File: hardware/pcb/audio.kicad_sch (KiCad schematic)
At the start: 7 parts, among them IC3 TAC5212, J6 PJ-342

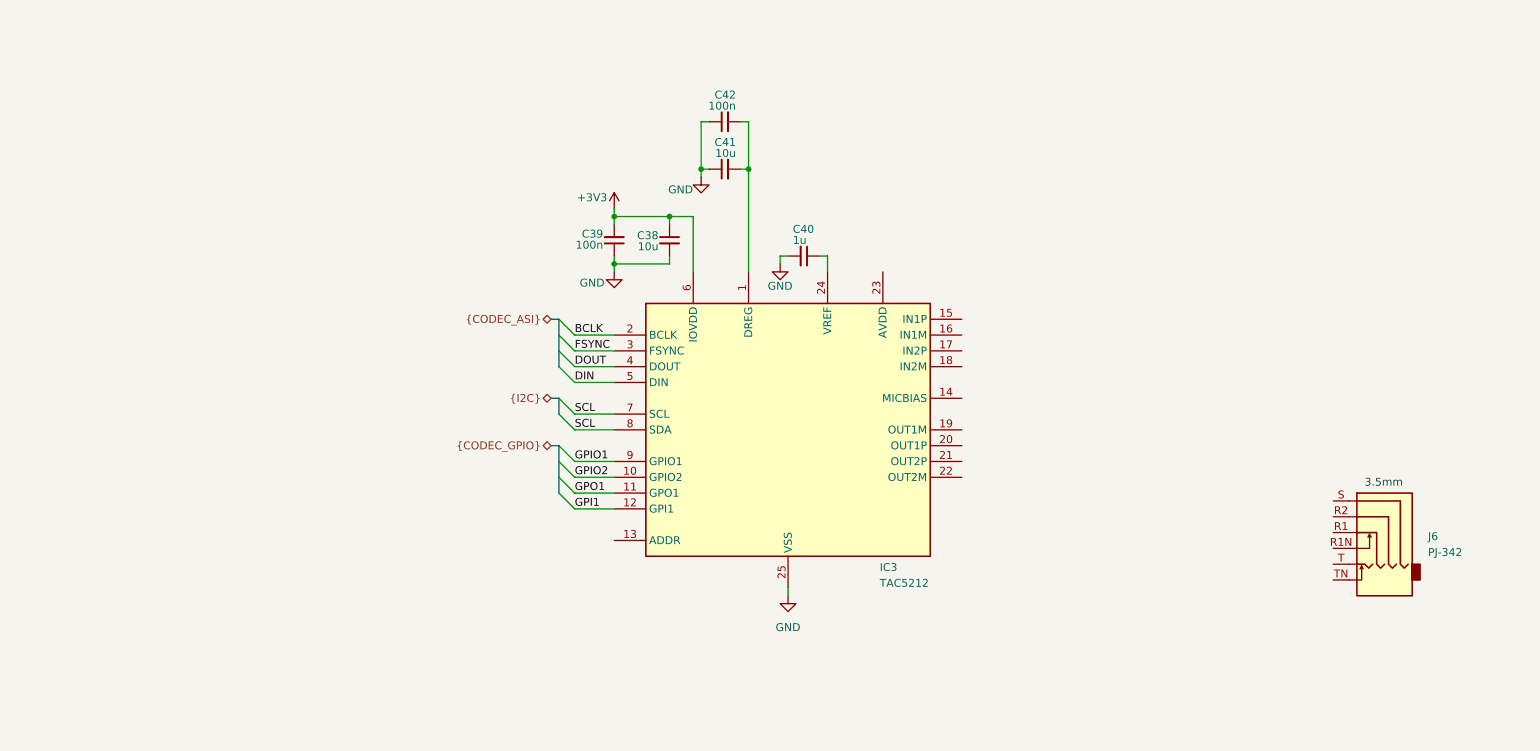
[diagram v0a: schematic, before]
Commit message: bunch of small audio changes
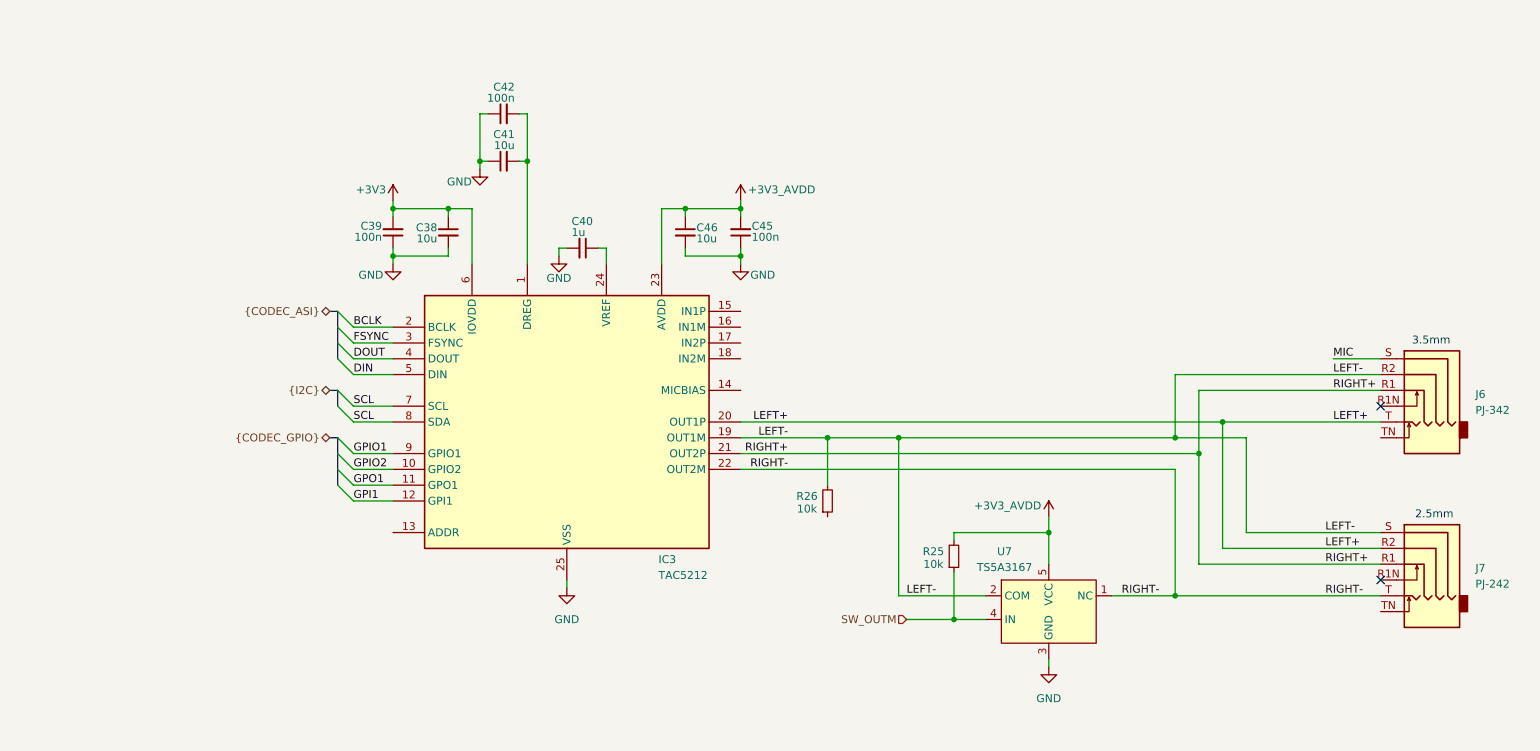
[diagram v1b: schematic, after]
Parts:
- added C45: 100n, symbol Device:C_Small
- added C46: 10u, symbol Device:C_Small
- added J7: PJ-242, PJ242:Jack_2.5mm_PJ242_6P_12x6.2x4mm_Horizontal, symbol Connector_Audio:AudioJack4_SwitchTR1
- added R25, R26: 10k, symbol Device:R_Small
- added U7: TS5A3167, Package_TO_SOT_SMD:SOT-23-5, symbol TS5A3167:TS5A3167
- J6: LCSC (none) -> C668606
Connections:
- net GND: now also C45.1, C46.2, U7.3 (GND)
- net RIGHT+: now reaches J6.R1
- net RIGHT+: now also IC3.21 (OUT2P), J7.R1
- net LEFT-: now reaches J6.R2
- net LEFT-: now also IC3.19 (OUT1M), J7.S, R26.2, U7.2 (COM)
- net MIC: now reaches J6.S
- net LEFT+: now reaches J6.T
- net LEFT+: now also IC3.20 (OUT1P), J7.R2
- net RIGHT-: now reaches IC3.22 (OUT2M)
- net RIGHT-: now also J7.T, U7.1 (NC)
- net +3V3_AVDD: now reaches IC3.23 (AVDD)
- net +3V3_AVDD: now also C45.2, C46.1, R25.2, U7.5 (VCC)
- new net SW_OUTM: R25.1, U7.4 (IN)
- no-connect marks 0 -> 2
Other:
- note added: "2.5mm"
- moved on the sheet: C38, C39, C40, C41, C42, IC3, J6

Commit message: bunch of small audio changes
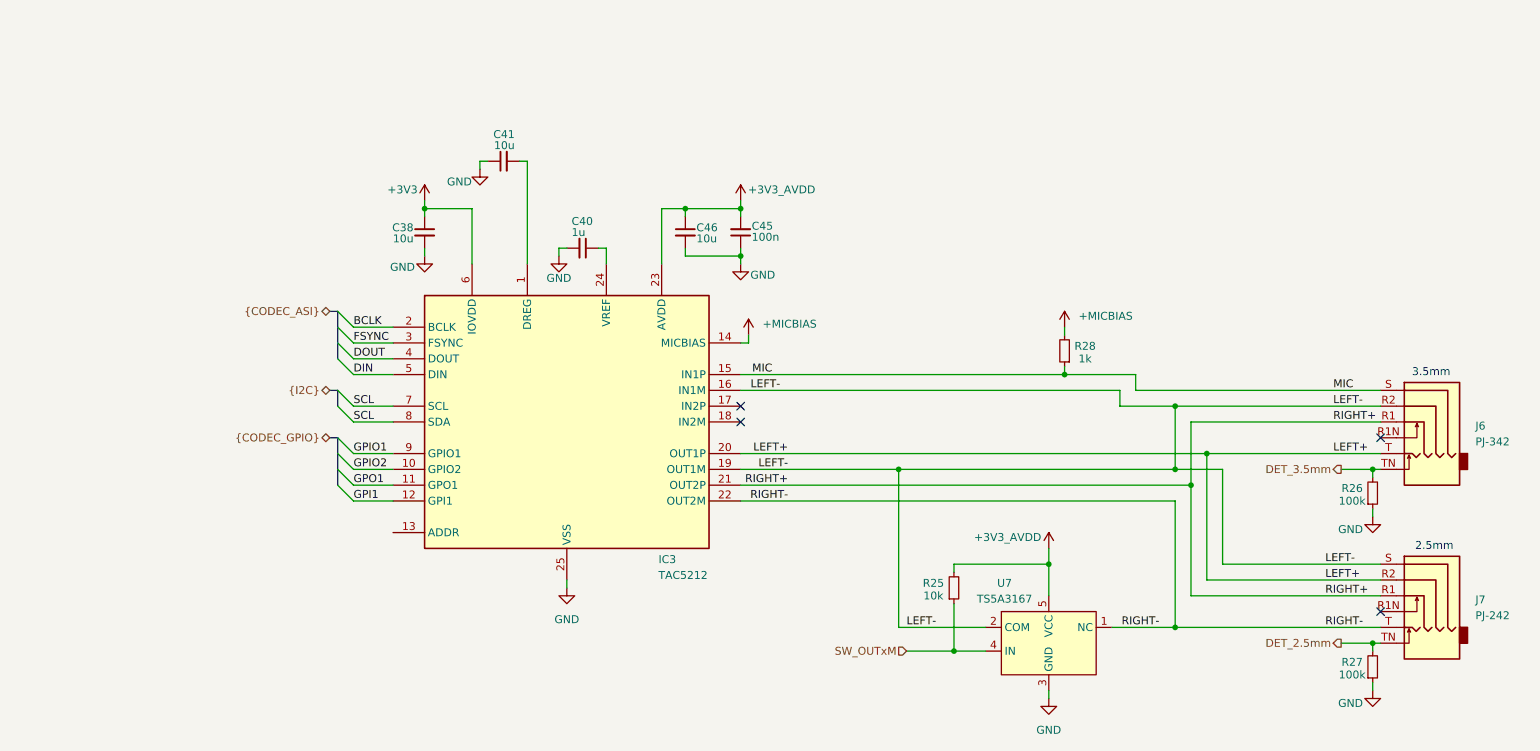
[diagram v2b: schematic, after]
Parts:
- removed C39, C42: 100n, symbol Device:C_Small
- added R27: 100k, symbol Device:R_Small
- added R28: 1k, symbol Device:R_Small
- R26: value 10k -> 100k
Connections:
- net GND: now also R26.1, R27.1
- net LEFT-: now also IC3.16 (IN1M); no longer R26.2
- net MIC: now also IC3.15 (IN1P), R28.1
- net DET_2.5mm: now reaches J7.TN
- net DET_2.5mm: now also R27.2
- net DET_3.5mm: now reaches J6.TN
- net DET_3.5mm: now also R26.2
- net +MICBIAS: now reaches IC3.14 (MICBIAS)
- net +MICBIAS: now also R28.2
- net SW_OUTM renamed SW_OUTxM
- no-connect marks 2 -> 4
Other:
- moved on the sheet: C38, J6, J7, R25, U7

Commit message: bunch of small audio and rf changes
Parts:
- removed C45: 100n, symbol Device:C_Small
- C38, C41: value 10u -> 1u
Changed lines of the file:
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@@
 	)
 	(junction
-		(at 134.62 58.42)
-		(diameter 0)
-		(color 0 0 0 0)
-	)
-	(junction
 		(at 204.47 92.71)
 		(diameter 0)
@@
 	)
 	(junction
-		(at 134.62 50.8)
-		(diameter 0)
-		(color 0 0 0 0)
-	)
-	(junction
 		(at 209.55 90.17)
 		(diameter 0)
@@
 	(wire
 		(pts
-			(xy 134.62 57.15) (xy 134.62 58.42)
-		)
-		(stroke
-			(width 0)
-			(type default)
-		)
-	)
-	(wire
-		(pts
 			(xy 134.62 92.71) (xy 160.02 92.71)
 		)
@@
 	(wire
 		(pts
-			(xy 134.62 49.53) (xy 134.62 50.8)
+			(xy 125.73 49.53) (xy 125.73 50.8)
 		)
 		(stroke
@@
 	(wire
 		(pts
-			(xy 125.73 58.42) (xy 125.73 57.15)
+			(xy 125.73 57.15) (xy 125.73 58.42)
 		)
 		(stroke
@@
 	(wire
 		(pts
-			(xy 134.62 59.69) (xy 134.62 58.42)
-		)
-		(stroke
-			(width 0)
-			(type default)
-		)
-	)
-	(wire
-		(pts
 			(xy 231.14 92.71) (xy 236.22 92.71)
 		)
@@
 		)
 	)
-	(wire
-		(pts
-			(xy 134.62 50.8) (xy 134.62 52.07)
-		)
-		(stroke
-			(width 0)
-			(type default)
-		)
-	)
 	(bus
 		(pts
@@
 	(wire
 		(pts
-			(xy 125.73 50.8) (xy 134.62 50.8)
-		)
-		(stroke
-			(width 0)
-			(type default)
-		)
-	)
-	(wire
-		(pts
 			(xy 207.01 85.09) (xy 237.49 85.09)
 		)
@@
 		)
 	)
-	(wire
-		(pts
-			(xy 134.62 58.42) (xy 125.73 58.42)
-		)
-		(stroke
-			(width 0)
-			(type default)
-		)
-	)
 	(bus
 		(pts
@@
 		)
 	)
-	(hierarchical_label "{CODEC_ASI}"
+	(hierarchical_label "{ASI}"
 		(shape bidirectional)
 		(at 68.58 67.31 180)
@@
 			)
 		)
-		(property "Value" "10u"
+		(property "Value" "1u"
 			(at 98.298 40.64 90)
 			(show_name no)
@@
 	(symbol
 		(lib_id "power:+3V3")
-		(at 134.62 49.53 0)
+		(at 125.73 49.53 0)
 		(unit 1)
 		(body_style 1)
@@
 		(dnp no)
 		(property "Reference" "#PWR094"
-			(at 134.62 53.34 0)
+			(at 125.73 53.34 0)
 			(hide yes)
 			(show_name no)
@@
 		)
 		(property "Value" "+3V3_AVDD"
-			(at 141.224 47.752 0)
+			(at 132.334 47.752 0)
 			(show_name no)
 			(do_not_autoplace no)
@@
 		)
 		(property "Footprint" ""
-			(at 134.62 49.53 0)
+			(at 125.73 49.53 0)
 			(hide yes)
 			(show_name no)
@@
 		)
 		(property "Datasheet" ""
-			(at 134.62 49.53 0)
+			(at 125.73 49.53 0)
 			(hide yes)
 			(show_name no)
@@
 		)
 		(property "Description" "Power symbol creates a global label with name \"+3V3\""
-			(at 134.62 49.53 0)
+			(at 125.73 49.53 0)
 			(hide yes)
 			(show_name no)
@@
 			)
 		)
-		(property "Value" "10u"
+		(property "Value" "1u"
 			(at 82.042 55.626 0)
 			(show_name no)
@@
 	(symbol
 		(lib_id "power:GND")
-		(at 134.62 59.69 0)
+		(at 125.73 58.42 0)
 		(mirror y)
 		(unit 1)
@@
 		(dnp no)
 		(property "Reference" "#PWR096"
-			(at 134.62 66.04 0)
+			(at 125.73 64.77 0)
 			(hide yes)
 			(show_name no)
@@
 		)
 		(property "Value" "GND"
-			(at 138.176 61.468 0)
+			(at 129.286 60.198 0)
 			(show_name no)
 			(do_not_autoplace no)
@@
 		)
 		(property "Footprint" ""
-			(at 134.62 59.69 0)
+			(at 125.73 58.42 0)
 			(hide yes)
 			(show_name no)
@@
 		)
 		(property "Datasheet" ""
-			(at 134.62 59.69 0)
+			(at 125.73 58.42 0)
 			(hide yes)
 			(show_name no)
@@
 		)
 		(property "Description" "Power symbol creates a global label with name \"GND\" , ground"
-			(at 134.62 59.69 0)
+			(at 125.73 58.42 0)
 			(hide yes)
 			(show_name no)
@@
 					(unit 1)
 				)
-			)
-		)
-	)
-	(symbol
-		(lib_id "Device:C_Small")
-		(at 134.62 54.61 0)
-		(mirror x)
-		(unit 1)
-		(body_style 1)
-		(exclude_from_sim no)
-		(in_bom yes)
-		(on_board yes)
-		(in_pos_files yes)
-		(dnp no)
-		(property "Reference" "C45"
-			(at 136.398 53.594 0)
-			(show_name no)
-			(do_not_autoplace no)
-			(effects
-				(font
-					(size 1.27 1.27)
-				)
-				(justify left)
-			)
-		)
-		(property "Value" "100n"
-			(at 136.398 55.372 0)
-			(show_name no)
-			(do_not_autoplace no)
-			(effects
-				(font
-					(size 1.27 1.27)
-				)
-				(justify left)
-			)
-		)
-		(property "Footprint" ""
-			(at 134.62 54.61 0)
-			(hide yes)
-			(show_name no)
-			(do_not_autoplace no)
-			(effects
-				(font
-					(size 1.27 1.27)
-				)
-			)
-		)
-		(property "Datasheet" ""
-			(at 134.62 54.61 0)
-			(hide yes)
-			(show_name no)
-			(do_not_autoplace no)
-			(effects
-				(font
-					(size 1.27 1.27)
-				)
-			)
-		)
-		(property "Description" "Unpolarized capacitor, small symbol"
-			(at 134.62 54.61 0)
-			(hide yes)
-			(show_name no)
-			(do_not_autoplace no)
-			(effects
-				(font
-					(size 1.27 1.27)
-				)
-			)
-		)
-		(property "KLC_S3.3" ""
-			(at 134.62 54.61 90)
-			(hide yes)
-			(show_name no)
-			(do_not_autoplace no)
-			(effects
-				(font
-					(size 1.27 1.27)
-				)
-			)
-		)
-		(property "KLC_S4.1" ""
-			(at 134.62 54.61 90)
-			(hide yes)
-			(show_name no)
-			(do_not_autoplace no)
-			(effects
-				(font
-					(size 1.27 1.27)
-				)
-			)
-		)
-		(pin "1"
-		)
-		(pin "2"
-		)
-		(instances
-			(project "meko"
-				(path "/da54f10a-146b-4941-a9c7-55c7173bb101/073f6085-34ed-486a-9dc9-0ac1ede2fab6"
-					(reference "C45")
-					(unit 1)
-				)

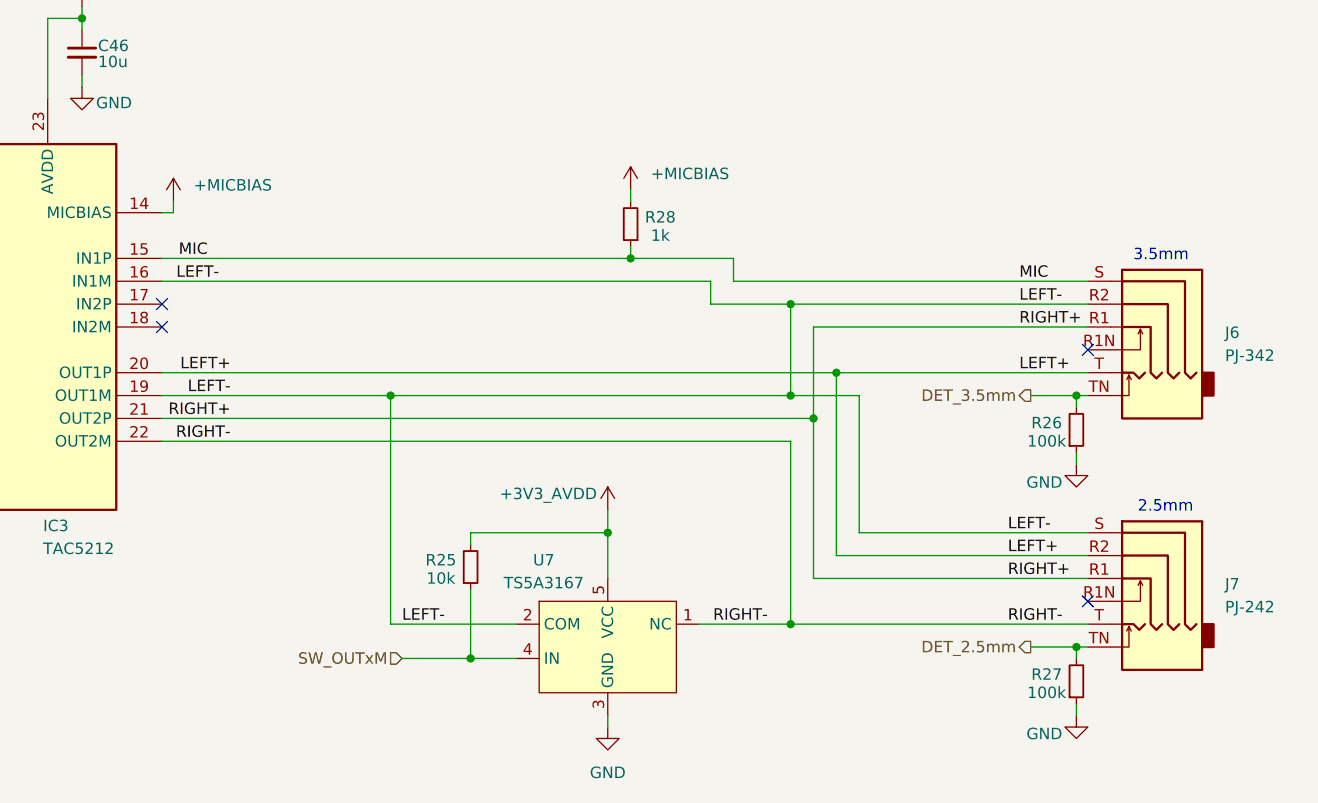
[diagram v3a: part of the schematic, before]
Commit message: removed analog switch from audio path
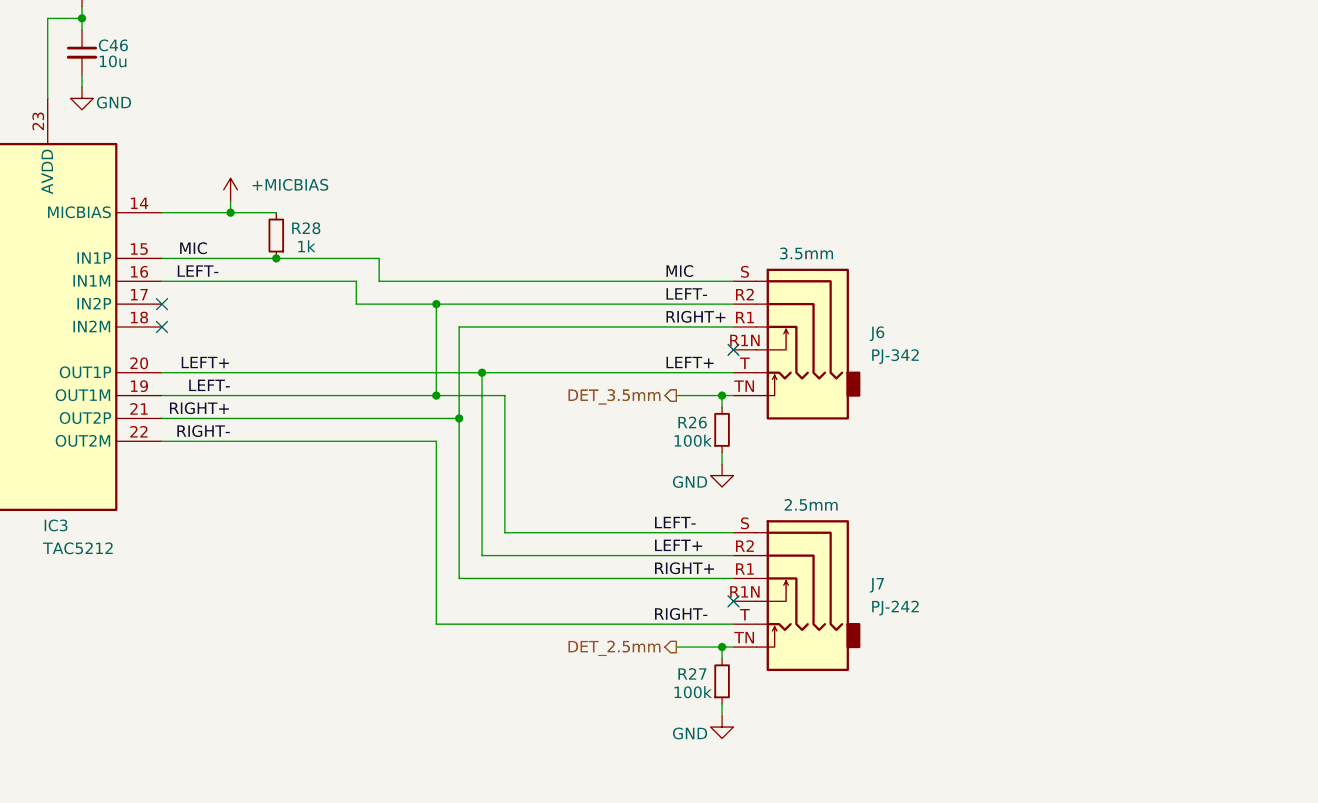
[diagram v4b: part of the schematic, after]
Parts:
- removed R25: 10k, symbol Device:R_Small
- removed U7: TS5A3167, Package_TO_SOT_SMD:SOT-23-5, symbol TS5A3167:TS5A3167
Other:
- moved on the sheet: J6, J7, R26, R27, R28

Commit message: small changes
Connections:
- net GND: now also IC3.13 (ADDR)
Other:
- note added: "0x50"
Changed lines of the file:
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@@
+		)
+	)
+	(text "0x50"
+		(exclude_from_sim no)
+		(at 59.436 80.518 0)
+		(effects
+			(font
+				(size 1.27 1.27)
+			)
 		)
 	)
@@
 	(wire
 		(pts
+			(xy 77.47 104.14) (xy 77.47 102.87)
+		)
+		(stroke
+			(width 0)
+			(type default)
+		)
+	)
+	(wire
+		(pts
 			(xy 158.75 77.47) (xy 158.75 80.01)
 		)
@@
 		(pts
 			(xy 72.39 82.55) (xy 78.74 82.55)
+		)
+		(stroke
+			(width 0)
+			(type default)
+		)
+	)
+	(wire
+		(pts
+			(xy 77.47 102.87) (xy 78.74 102.87)
 		)
 		(stroke
@@
 					(unit 1)
 				)
+			)
+		)
+	)
+	(symbol
+		(lib_id "power:GND")
+		(at 77.47 104.14 0)
+		(unit 1)
+		(body_style 1)
+		(exclude_from_sim no)
+		(in_bom yes)
+		(on_board yes)
+		(in_pos_files yes)
+		(dnp no)
+		(fields_autoplaced yes)
+		(property "Reference" "#PWR095"
+			(at 77.47 110.49 0)
+			(hide yes)
+			(show_name no)
+			(do_not_autoplace no)
+			(effects
+				(font
+					(size 1.27 1.27)
+				)
+			)
+		)
+		(property "Value" "GND"
+			(at 77.47 109.22 0)
+			(show_name no)
+			(do_not_autoplace no)
+			(effects
+				(font
+					(size 1.27 1.27)
+				)
+			)
+		)
+		(property "Footprint" ""
+			(at 77.47 104.14 0)
+			(hide yes)
+			(show_name no)
+			(do_not_autoplace no)
+			(effects
+				(font
+					(size 1.27 1.27)
+				)
+			)
+		)
+		(property "Datasheet" ""
+			(at 77.47 104.14 0)
+			(hide yes)
+			(show_name no)
+			(do_not_autoplace no)
+			(effects
+				(font
+					(size 1.27 1.27)
+				)
+			)
+		)
+		(property "Description" "Power symbol creates a global label with name \"GND\" , ground"
+			(at 77.47 104.14 0)
+			(hide yes)
+			(show_name no)
+			(do_not_autoplace no)
+			(effects
+				(font
+					(size 1.27 1.27)
+				)
+			)
+		)
+		(pin "1"
+		)
+		(instances
+			(project "meko"
+				(path "/da54f10a-146b-4941-a9c7-55c7173bb101/073f6085-34ed-486a-9dc9-0ac1ede2fab6"
+					(reference "#PWR095")
+					(unit 1)
+				)

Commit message: assigning pins
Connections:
- net DET_2.5mm renamed ~{DET}_2.5mm
- net DET_3.5mm renamed ~{DET}_3.5mm
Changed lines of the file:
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@@
 		)
 	)
-	(hierarchical_label "DET_3.5mm"
+	(hierarchical_label "~{DET}_3.5mm"
 		(shape output)
 		(at 191.77 92.71 180)
@@
 		)
 	)
-	(hierarchical_label "DET_2.5mm"
+	(hierarchical_label "~{DET}_2.5mm"
 		(shape output)
 		(at 191.77 120.65 180)

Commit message: looking over stuff, added caps
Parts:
- removed C38, C40: 1u, symbol Device:C_Small
- added C45: 10u, Capacitor_SMD:C_0402_1005Metric, symbol Device:C_Small
- added C47: 1u, Capacitor_SMD:C_0402_1005Metric, symbol Device:C_Small
- C41, C46: footprint (none) -> Capacitor_SMD:C_0402_1005Metric
- R26, R27, R28: footprint (none) -> Resistor_SMD:R_0402_1005Metric
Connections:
- net +3V3: now also C45.2
- net +3V3_AVDD: now also C46.2; no longer C46.1
- net GND: now also C46.1, C45.1, C47.1; no longer C46.2
- net SCL: no longer IC3.8 (SDA)
- net at IC3.24 (VREF): now also C47.2
- new net SDA: IC3.8 (SDA)
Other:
- moved on the sheet: C41, IC3, J6, J7, R26, R27, R28

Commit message: started cleaning up schematic
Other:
- company: (none) -> Gensis
- title: (none) -> Audio
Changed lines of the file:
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@@
 	(generator_version "10.0")
 	(paper "A5")
+	(title_block
+		(title "Audio")
+		(rev "v1.0.0")
+		(company "Gensis")
+	)
 	(text "3.5mm"
 		(exclude_from_sim no)
